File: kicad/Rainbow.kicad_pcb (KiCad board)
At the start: 2 copper layers, 53.2 x 38.7 mm, 22 parts, among them J1 PICKit3, J2 USB SERIAL, J3 JUMPER, J4 JACK, J5 RGB, J6 RGB, J7 RGB, J8 RGB, J9 SOURCE, Q1 2N7000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

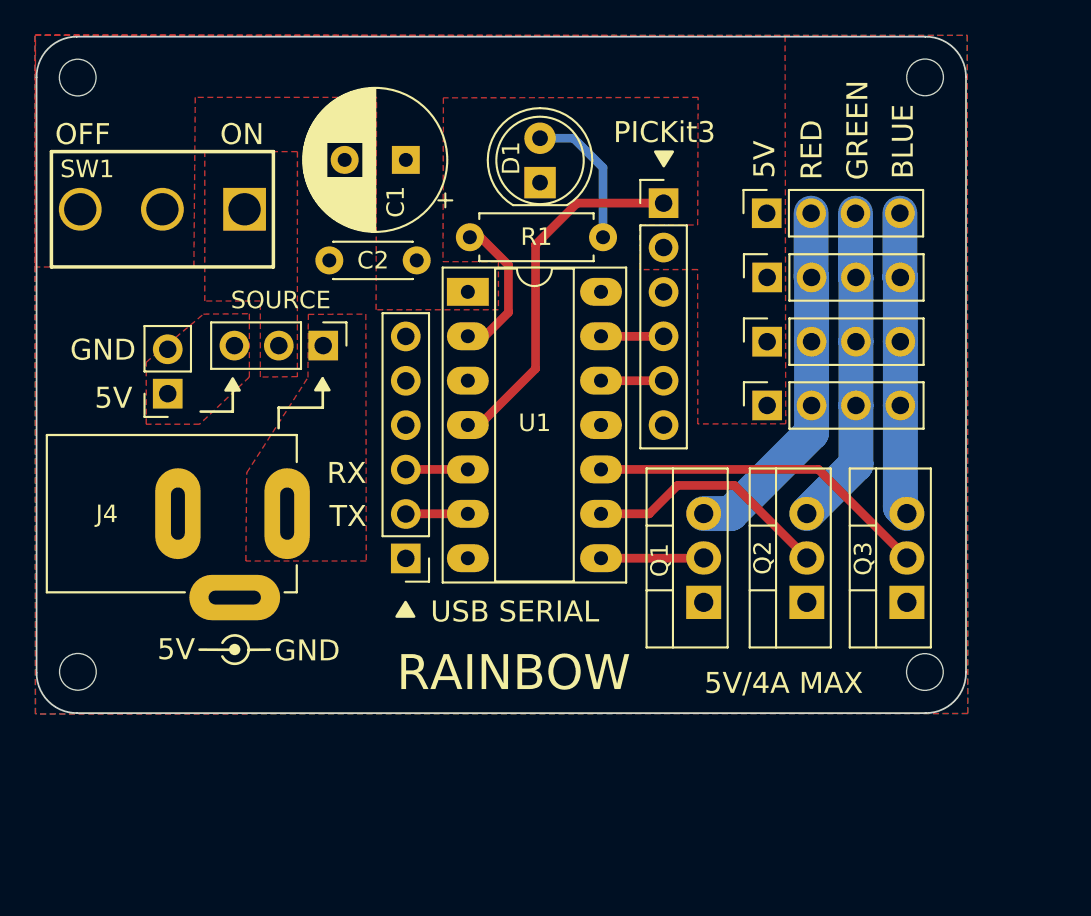
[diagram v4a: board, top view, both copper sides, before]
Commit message: tweak silk and placement
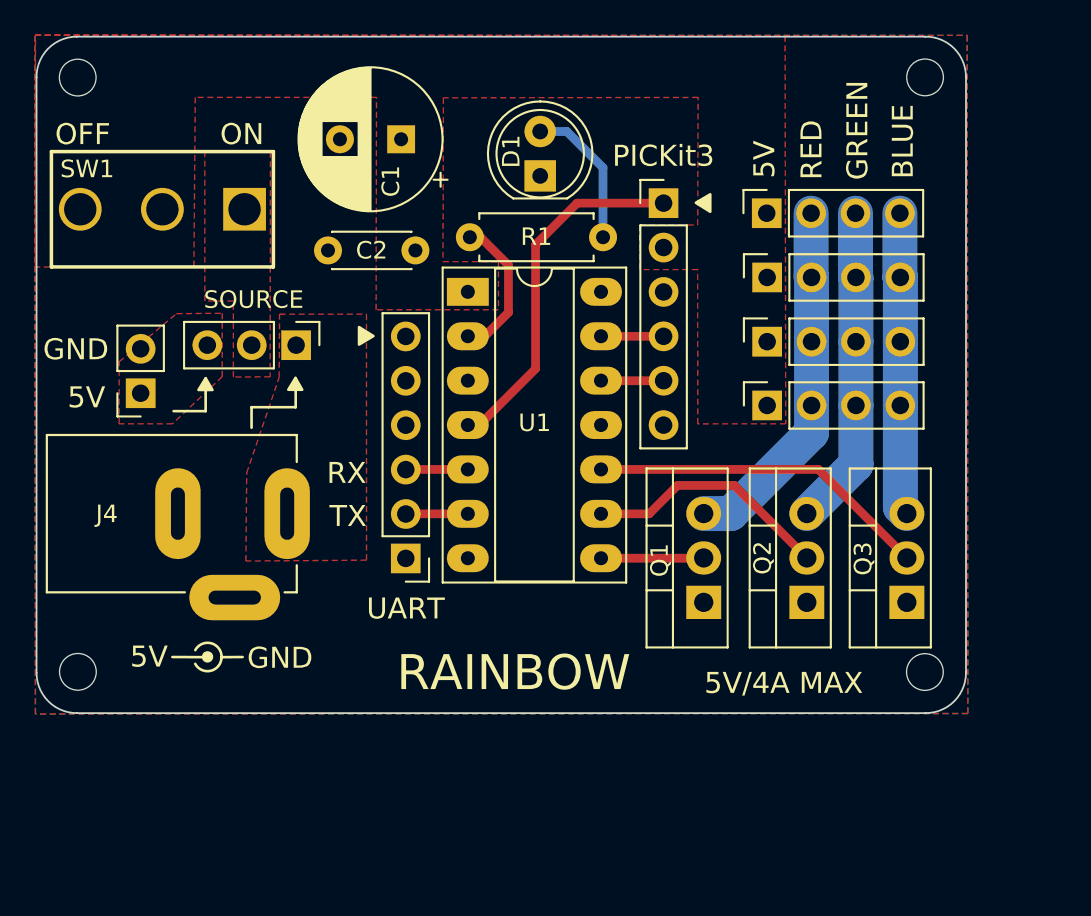
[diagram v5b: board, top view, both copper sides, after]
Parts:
- moved J3 1.55 mm to (95.4, 79.7)
- moved J9 1.55 mm to (104.3, 77.0)
- moved C1 1.21 mm to (110.3, 65.2)
- moved C2 0.57 mm to (111.2, 71.5)
- moved D1 0.39 mm to (118.3, 67.3)
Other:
- board text added: "UART"
- board text removed: "USB SERIAL"
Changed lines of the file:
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@@
   )
   (footprint "Capacitor_THT:C_Disc_D4.3mm_W1.9mm_P5.00mm" (layer "F.Cu")
-    (at 111.225 72.1 180)
+    (at 111.15 71.53 180)
     (descr "C, Disc series, Radial, pin pitch=5.00mm, , diameter*width=4.3*1.9mm^2, Capacitor, http://www.vishay.com/docs/45233/krseries.pdf")
     (tags "C Disc series Radial pin pitch 5.00mm  diameter 4.3mm width 1.9mm Capacitor")
@@
   )
   (footprint "LED_THT:LED_D5.0mm" (layer "F.Cu")
-    (at 118.28 67.65 90)
+    (at 118.29 67.265 90)
     (descr "LED, diameter 5.0mm, 2 pins, http://cdn-reichelt.de/documents/datenblatt/A500/LL-504BC2E-009.pdf")
     (tags "LED diameter 5.0mm 2 pins")
@@
   )
   (footprint "Capacitor_THT:CP_Radial_D8.0mm_P3.50mm" (layer "F.Cu")
-    (at 110.602651 66.35 180)
+    (at 110.332651 65.17 180)
     (descr "CP, Radial series, Radial, pin pitch=3.50mm, , diameter=8mm, Electrolytic Capacitor")
     (tags "CP Radial series Radial pin pitch 3.50mm  diameter 8mm Electrolytic Capacitor")
@@
   )
   (footprint "Connector_PinHeader_2.54mm:PinHeader_1x03_P2.54mm_Vertical" (layer "F.Cu")
-    (at 105.875 76.975 -90)
+    (at 104.325 76.95 -90)
     (descr "Through hole straight pin header, 1x03, 2.54mm pitch, single row")
     (tags "Through hole pin header THT 1x03 2.54mm single row")
@@
   )
   (footprint "Connector_PinSocket_2.54mm:PinSocket_1x02_P2.54mm_Vertical" (layer "F.Cu")
-    (at 96.98 79.725 180)
+    (at 95.43 79.7 180)
     (descr "Through hole straight socket strip, 1x02, 2.54mm pitch, single row (from Kicad 4.0.7), script generated")
     (tags "Through hole socket strip THT 1x02 2.54mm single row")
@@
     (pad "" np_thru_hole circle (at 0 0) (size 2.1 2.1) (drill 2.1) (layers *.Cu *.Mask))
   )
-  (gr_line (start 100.7 80.75) (end 100.7 78.875) (layer "F.SilkS") (width 0.15))
-  (gr_arc (start 101.61 94.38) (mid 101.004747 95.155934) (end 100.104816 94.757777) (layer "F.SilkS") (width 0.15))
-  (gr_line (start 98.8625 80.75) (end 100.7 80.75) (layer "F.SilkS") (width 0.15))
+  (gr_line (start 99.15 80.725) (end 99.15 78.85) (layer "F.SilkS") (width 0.15))
+  (gr_arc (start 100.055184 94.802223) (mid 99.449931 95.578157) (end 98.55 95.18) (layer "F.SilkS") (width 0.15))
+  (gr_line (start 97.3125 80.725) (end 99.15 80.725) (layer "F.SilkS") (width 0.15))
   (gr_poly
     (pts
-      (xy 111.075 92.475)
-      (xy 110.075 92.475)
-      (xy 110.58844 91.65)
+      (xy 107.925 76.91656)
+      (xy 107.925 75.91656)
+      (xy 108.75 76.43)
     ) (layer "F.SilkS") (width 0.15) (fill solid))
-  (gr_line (start 98.8 94.37) (end 100.81 94.38) (layer "F.SilkS") (width 0.15))
-  (gr_line (start 103.325 81.7) (end 103.325 80.525) (layer "F.SilkS") (width 0.15))
-  (gr_arc (start 100.110069 93.978157) (mid 101.009971 93.580114) (end 101.615253 94.355934) (layer "F.SilkS") (width 0.15))
+  (gr_line (start 97.245184 94.792223) (end 99.255184 94.802223) (layer "F.SilkS") (width 0.15))
+  (gr_line (start 101.775 81.675) (end 101.775 80.5) (layer "F.SilkS") (width 0.15))
+  (gr_arc (start 98.555253 94.40038) (mid 99.455155 94.002337) (end 100.060437 94.778157) (layer "F.SilkS") (width 0.15))
   (gr_poly
     (pts
-      (xy 124.87365 65.880807)
-      (xy 125.87365 65.880807)
-      (xy 125.36021 66.705807)
+      (xy 128.02 68.31844)
+      (xy 128.02 69.31844)
+      (xy 127.195 68.805)
     ) (layer "F.SilkS") (width 0.15) (fill solid))
   (gr_poly
     (pts
-      (xy 106.225 79.525)
-      (xy 105.425 79.525)
-      (xy 105.83844 78.85)
+      (xy 104.675 79.5)
+      (xy 103.875 79.5)
+      (xy 104.28844 78.825)
     ) (layer "F.SilkS") (width 0.15) (fill solid))
   (gr_poly
     (pts
-      (xy 101.087265 79.538137)
-      (xy 100.287265 79.538137)
-      (xy 100.700705 78.863137)
+      (xy 99.537265 79.513137)
+      (xy 98.737265 79.513137)
+      (xy 99.150705 78.838137)
     ) (layer "F.SilkS") (width 0.15) (fill solid))
-  (gr_line (start 101.61 94.38) (end 102.82 94.37) (layer "F.SilkS") (width 0.15))
-  (gr_line (start 103.325 80.525) (end 105.85 80.525) (layer "F.SilkS") (width 0.15))
-  (gr_circle (center 100.81 94.362688) (end 101.06 94.38) (layer "F.SilkS") (width 0.15) (fill solid))
-  (gr_line (start 105.85 78.85) (end 105.85 80.525) (layer "F.SilkS") (width 0.15))
+  (gr_line (start 100.055184 94.802223) (end 101.265184 94.792223) (layer "F.SilkS") (width 0.15))
+  (gr_line (start 101.775 80.5) (end 104.3 80.5) (layer "F.SilkS") (width 0.15))
+  (gr_circle (center 99.255184 94.784911) (end 99.505184 94.802223) (layer "F.SilkS") (width 0.15) (fill solid))
+  (gr_line (start 104.3 78.825) (end 104.3 80.5) (layer "F.SilkS") (width 0.15))
   (gr_arc (start 140.325 59.3) (mid 141.967491 59.964792) (end 142.65 61.6) (layer "Edge.Cuts") (width 0.1))
   (gr_line (start 140.325 59.3) (end 91.775 59.3) (layer "Edge.Cuts") (width 0.1))
@@
     (effects (font (size 1.2 1.2) (thickness 0.2)))
   )
-  (gr_text "PICKit3" (at 125.4 64.775) (layer "F.SilkS")
+  (gr_text "PICKit3" (at 125.34 66.13) (layer "F.SilkS")
     (effects (font (size 1.2 1.2) (thickness 0.2)))
   )
@@
     (effects (font (size 2 2) (thickness 0.5)))
   )
-  (gr_text "GND" (at 104.96 94.43) (layer "F.SilkS")
+  (gr_text "GND" (at 103.405184 94.852223) (layer "F.SilkS")
     (effects (font (size 1.2 1.2) (thickness 0.2)))
   )
@@
     (effects (font (size 1.2 1.2) (thickness 0.25)))
   )
-  (gr_text "USB SERIAL" (at 116.84 92.202) (layer "F.SilkS")
-    (effects (font (size 1.2 1.2) (thickness 0.2)))
-  )
-  (gr_text "GND" (at 93.275 77.225) (layer "F.SilkS")
-    (effects (font (size 1.2 1.2) (thickness 0.2)))
-  )
-  (gr_text "5V" (at 97.46 94.36) (layer "F.SilkS")
-    (effects (font (size 1.2 1.2) (thickness 0.2)))
-  )
-  (gr_text "SOURCE" (at 103.45 74.375) (layer "F.SilkS")
+  (gr_text "UART" (at 110.59 92.03) (layer "F.SilkS")
+    (effects (font (size 1.2 1.2) (thickness 0.2)))
+  )
+  (gr_text "GND" (at 91.725 77.2) (layer "F.SilkS")
+    (effects (font (size 1.2 1.2) (thickness 0.2)))
+  )
+  (gr_text "5V" (at 95.905184 94.782223) (layer "F.SilkS")
+    (effects (font (size 1.2 1.2) (thickness 0.2)))
+  )
+  (gr_text "SOURCE" (at 101.9 74.35) (layer "F.SilkS")
     (effects (font (size 1 1) (thickness 0.2)))
   )
@@
     (effects (font (size 1.2 1.2) (thickness 0.2)))
   )
-  (gr_text "5V" (at 93.875 79.975) (layer "F.SilkS")
+  (gr_text "5V" (at 92.325 79.95) (layer "F.SilkS")
     (effects (font (size 1.2 1.2) (thickness 0.2)))
   )
@@
     (effects (font (size 1.2 1.2) (thickness 0.2)))
   )
-  (segment (start 120.2 65.11) (end 118.28 65.11) (width 0.5) (layer "B.Cu") (net 2))
   (segment (start 121.885 70.775) (end 121.885 66.795) (width 0.5) (layer "B.Cu") (net 2))
-  (segment (start 121.885 66.795) (end 120.2 65.11) (width 0.5) (layer "B.Cu") (net 2))
+  (segment (start 119.815 64.725) (end 118.29 64.725) (width 0.5) (layer "B.Cu") (net 2))
+  (segment (start 121.885 66.795) (end 119.815 64.725) (width 0.5) (layer "B.Cu") (net 2))
   (segment (start 120.4 68.825) (end 118.025 71.2) (width 0.5) (layer "F.Cu") (net 3))
   (segment (start 118.025 78.3) (end 114.805 81.52) (width 0.5) (layer "F.Cu") (net 3))
@@
     (connect_pads (clearance 0.508))
     (min_thickness 0.254) (filled_areas_thickness no)
-    (fill yes (thermal_gap 0.508) (thermal_bridge_width 0.508))
+    (fill yes (thermal_gap 0.508) (thermal_bridge_width 0.508) (smoothing fillet) (radius 1))
     (polygon
       (pts
-        (xy 108.33962 89.298273)
+        (xy 108.353485 89.249988)
         (xy 101.450136 89.300135)
         (xy 101.5 84.25)
-        (xy 105.002968 78.799355)
-        (xy 105.024999 75.190225)
-        (xy 108.314484 75.173138)
+        (xy 103.356047 78.789301)
+        (xy 103.378078 75.180171)
+        (xy 108.347969 75.173126)
       )
     )
@@
     (connect_pads (clearance 0.508))
     (min_thickness 0.254) (filled_areas_thickness no)
-    (fill yes (thermal_gap 0.508) (thermal_bridge_width 0.508))
+    (fill yes (thermal_gap 0.508) (thermal_bridge_width 0.508) (smoothing fillet) (radius 1))
     (polygon
       (pts
@@
     (connect_pads (clearance 0.508))
     (min_thickness 0.254) (filled_areas_thickness no)
-    (fill yes (thermal_gap 0.508) (thermal_bridge_width 0.508))
+    (fill yes (thermal_gap 0.508) (thermal_bridge_width 0.508) (smoothing fillet) (radius 1))
     (polygon
       (pts
-        (xy 101.65 78.775)
-        (xy 98.8 81.475)
-        (xy 95.75 81.475)
-        (xy 95.75 77.925)
-        (xy 99.025 75.175)
-        (xy 101.65 75.15)
+        (xy 100.1 78.75)
+        (xy 97.25 81.45)
+        (xy 94.2 81.45)
+        (xy 94.2 77.9)
+        (xy 97.475 75.15)
+        (xy 100.1 75.125)
       )
     )
@@
     (connect_pads (clearance 0.508))
     (min_thickness 0.254) (filled_areas_thickness no)
-    (fill yes (thermal_gap 0.508) (thermal_bridge_width 0.508))
+    (fill yes (thermal_gap 0.508) (thermal_bridge_width 0.508) (smoothing fillet) (radius 1))
     (polygon
       (pts
@@
     (connect_pads (clearance 0.508))
     (min_thickness 0.254) (filled_areas_thickness no)
-    (fill yes (thermal_gap 0.508) (thermal_bridge_width 0.508))
+    (fill yes (thermal_gap 0.508) (thermal_bridge_width 0.508) (smoothing fillet) (radius 1))
     (polygon
       (pts
-        (xy 104.396196 78.750578)
-        (xy 102.275 78.775)
-        (xy 102.275 74.425)
+        (xy 102.84 78.76)
+        (xy 100.735 78.775)
+        (xy 100.735 74.425)
         (xy 99.1 74.425)
         (xy 99.1 65.875)
-        (xy 104.40081 65.874956)
+        (xy 102.853365 65.874402)
       )
     )

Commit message: Fix FET pins and traces
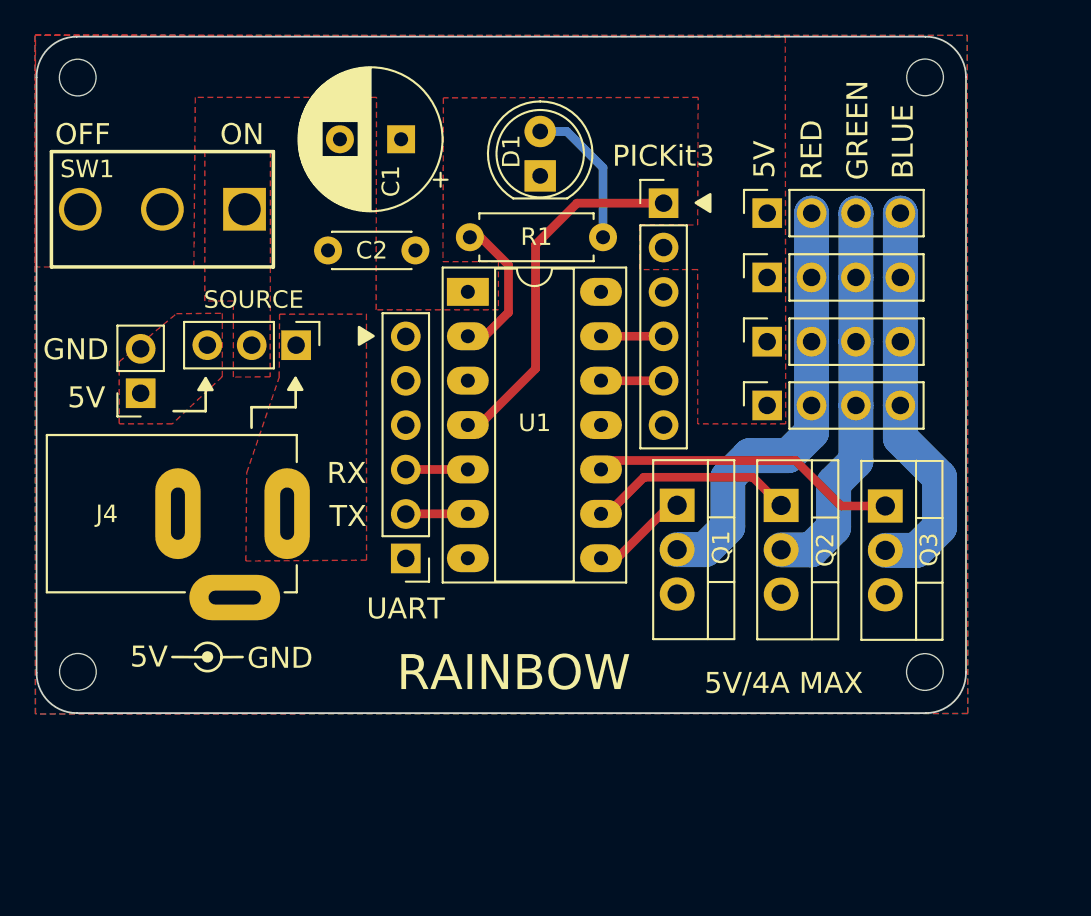
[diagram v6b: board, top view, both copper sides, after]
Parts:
- J2: value USB SERIAL -> UART
- Q1, Q2, Q3: value 2N7000 -> Q_NMOS_GDS
- moved Q1 5.76 mm to (126.1, 86.1), turned to -90 degrees
- moved Q2 5.74 mm to (132.1, 86.1), turned to -90 degrees
- moved Q3 5.65 mm to (138.0, 86.2), turned to -90 degrees
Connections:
- Q1 pad 1: GNDREF -> RED
- Q1 pad 2: RED -> Net-(J5-Pad2)
- Q1 pad 3: Net-(J5-Pad2) -> GNDREF
- Q2 pad 1: GNDREF -> GREEN
- Q2 pad 2: GREEN -> Net-(J5-Pad3)
- Q2 pad 3: Net-(J5-Pad3) -> GNDREF
- Q3 pad 1: GNDREF -> BLUE
- Q3 pad 2: BLUE -> Net-(J5-Pad4)
- Q3 pad 3: Net-(J5-Pad4) -> GNDREF
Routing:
- net Net-(J5-Pad4): track 17.4 -> 22.6 mm
- net Net-(J5-Pad2): track 20.7 -> 24.7 mm
- net Net-(J5-Pad3): track 18.4 -> 22.1 mm
- net BLUE: track 19.6 -> 16.8 mm
- net GREEN: track 14.2 -> 11.5 mm
- net RED: track 5.86 -> 4.29 mm
